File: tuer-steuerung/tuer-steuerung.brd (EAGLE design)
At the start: 65.7 x 67.3 mm, 47 parts, among them IC1 L6203, IC2 MEGA8-P, Q1 16Mhz, T1 BC337, T2 BC337

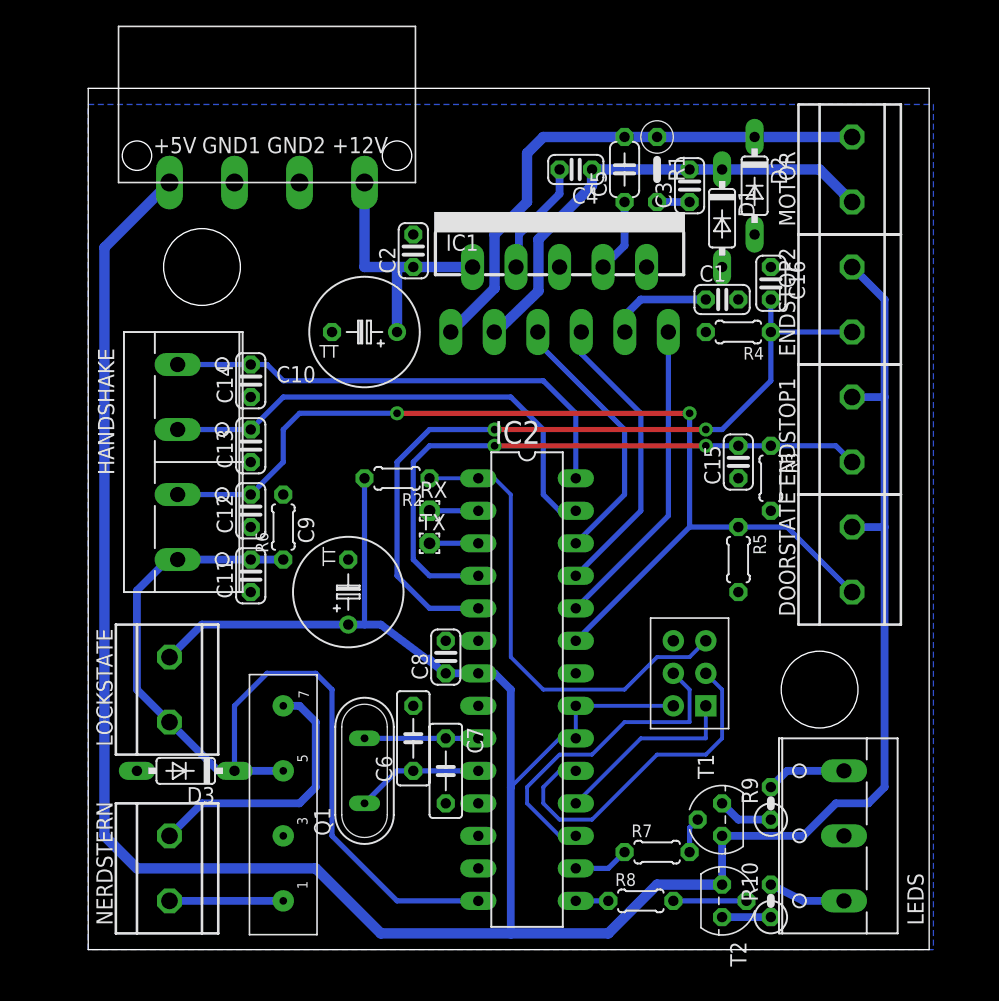
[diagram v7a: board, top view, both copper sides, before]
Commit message: Anschlussklemmen durch die richtigen Typen ersetzt und Mini-Tweaks
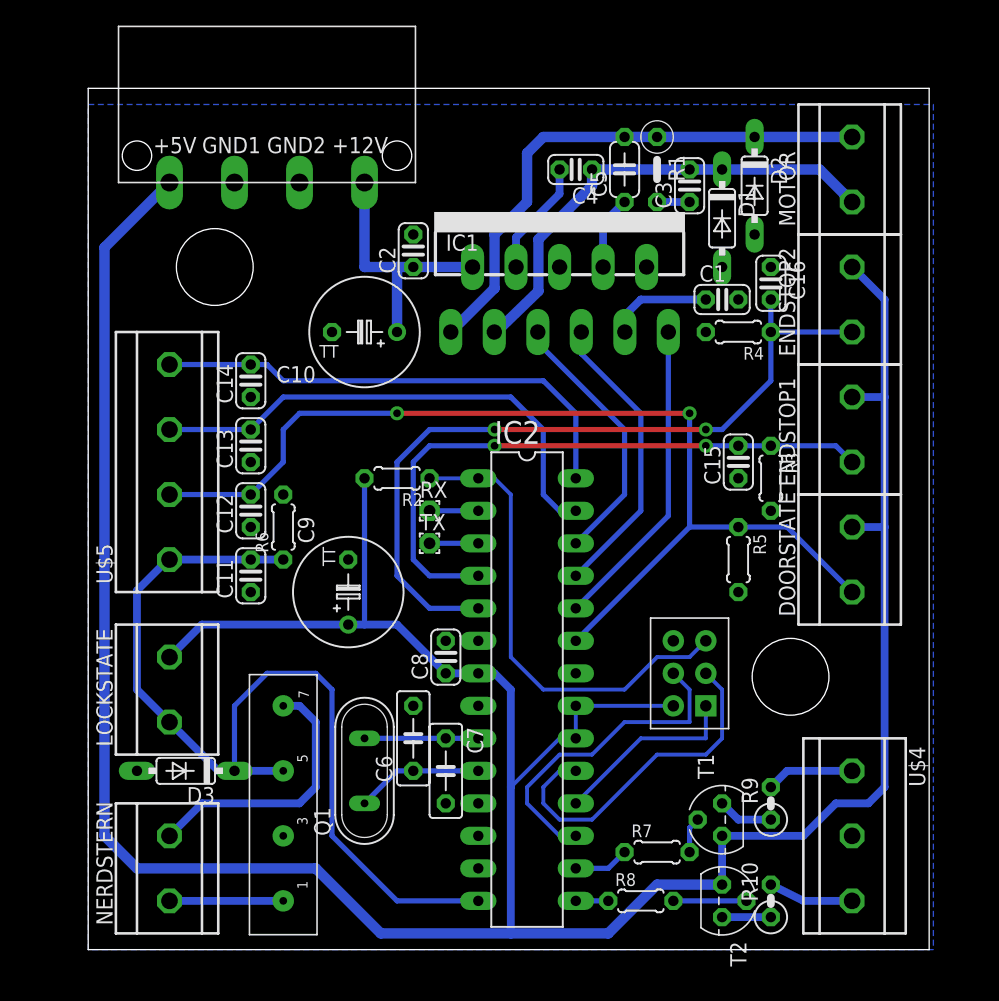
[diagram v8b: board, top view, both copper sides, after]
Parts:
- removed HANDSHAKE: (no value), con-wago-508:W237-4P
- removed LEDS: (no value), con-wago-508:W237-133
- added U$4: RIACON_101_3, n39:RIACON_101_3
- added U$5: RIACON_101_4, n39:RIACON_101_4
- D1, D2: value (none) -> BS170
- D3: value (none) -> 1N4148DO35-7
- R7, R8: value 470R -> 1,5K
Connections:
- net DOORSTATE: now also U$5.2; no longer HANDSHAKE.3
- net GND: now also U$4.2; no longer LEDS.2
- net LOCKSTATE: now also U$5.1; no longer HANDSHAKE.4
- net N$12: now also U$4.1; no longer LEDS.3
- net N$14: now also U$4.3; no longer LEDS.1
- net SET_CLOSE: now also U$5.3; no longer HANDSHAKE.2
- net SET_OPEN: now also U$5.4; no longer HANDSHAKE.1
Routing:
- net VCC: track 249.6 -> 248.1 mm
- net SET_OPEN: track 37.8 -> 38.4 mm
- net SET_CLOSE: track 38.8 -> 39.5 mm
- net N$14: track 6.01 -> 6.65 mm
- net N$12: track 6.24 -> 6.88 mm
- net DOORSTATE: track 80.4 -> 81.0 mm
